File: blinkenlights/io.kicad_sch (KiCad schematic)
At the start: 23 parts, among them J501 Conn_02x10_Odd_Even, U501 XRA1403, U502 PCA9306DP, U503 XRA1403, U504 XRA1402

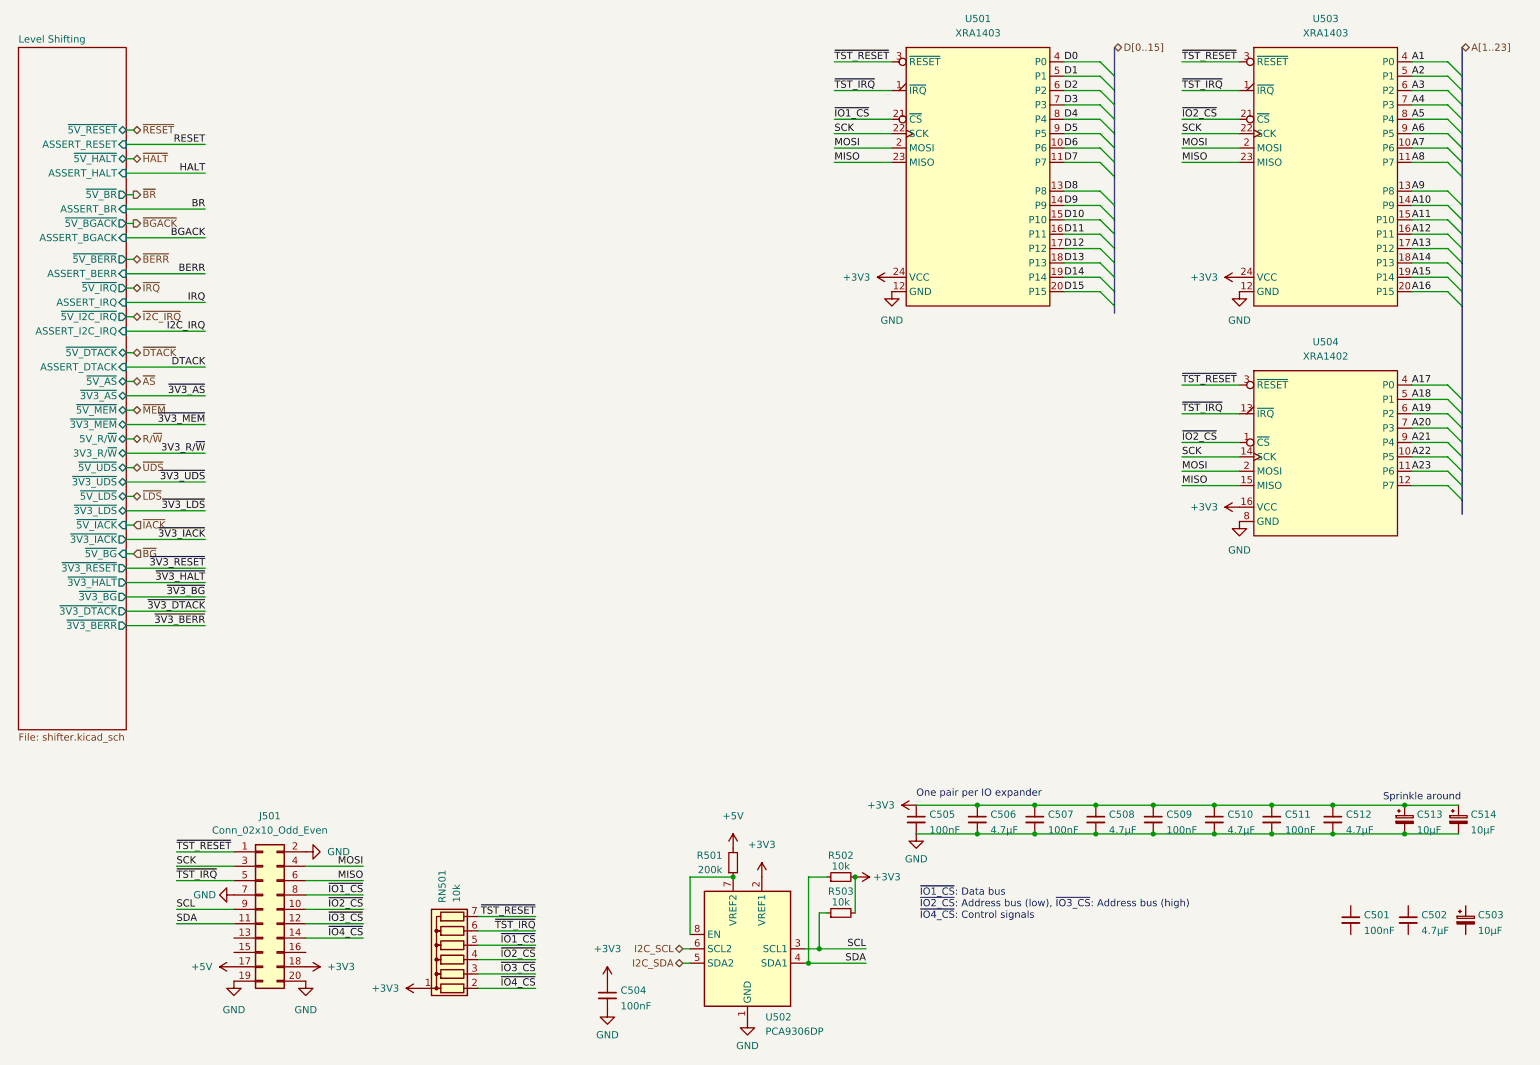
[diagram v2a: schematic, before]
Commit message: Routed control signals
- The blinkenlights board now has the control signals routed to IO
  expanders, and removed a bunch of superfluous level shifting type
  stuff
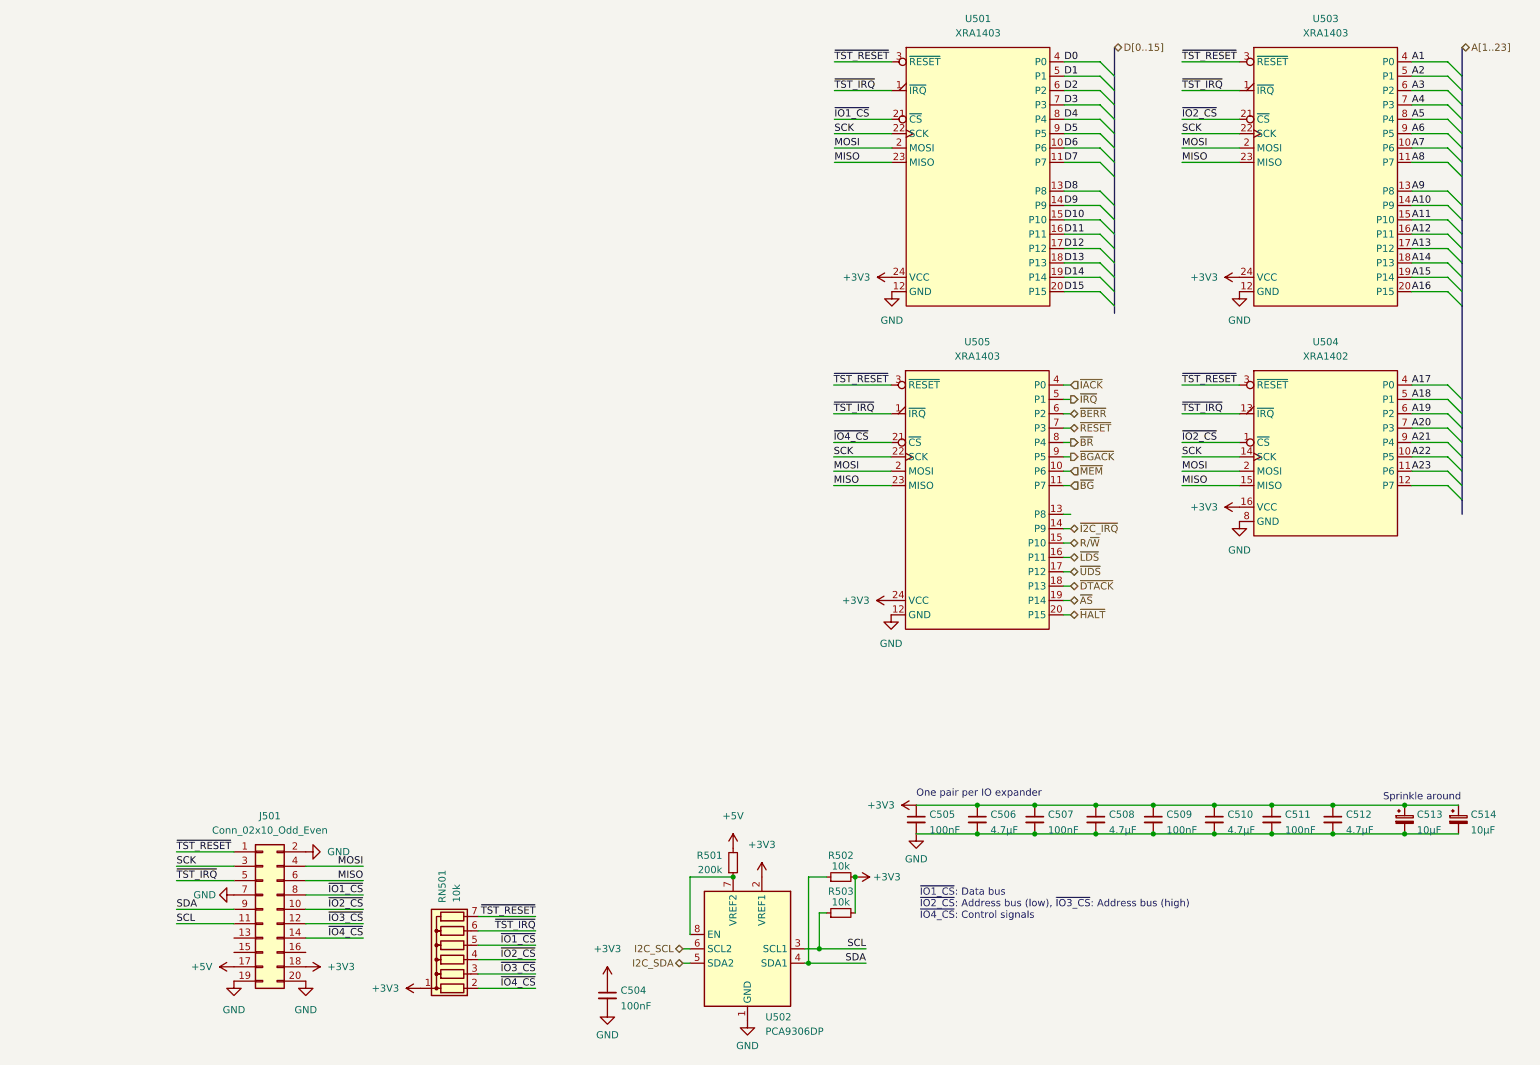
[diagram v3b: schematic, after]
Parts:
- removed C501: 100nF, Capacitor_SMD:C_0805_2012Metric, symbol Device:C_Small
- removed C502: 4.7µF, Capacitor_SMD:C_0805_2012Metric, symbol Device:C_Small
- removed C503: 10µF, Capacitor_Tantalum_SMD:CP_EIA-3528-21_Kemet-B, symbol Device:C_Polarized_Small
- added U505: XRA1403, Package_SO:TSSOP-24_4.4x7.8mm_P0.65mm, symbol 68komputer-common:XRA1403
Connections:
- net +3V3: now also U505.24 (VCC)
- net GND: now also U505.12 (GND)
- net MISO: now also U505.23 (MISO)
- net MOSI: now also U505.2 (MOSI)
- net R/~{W}: now also U505.15 (P10)
- net SCK: now also U505.22 (SCK)
- net SCL: now also J501.11 (Pin_11); no longer J501.9 (Pin_9)
- net SDA: now also J501.9 (Pin_9); no longer J501.11 (Pin_11)
- net ~{AS}: now also U505.19 (P14)
- net ~{BERR}: now also U505.6 (P2)
- net ~{BGACK}: now also U505.9 (P5)
- net ~{BG}: now also U505.11 (P7)
- net ~{BR}: now also U505.8 (P4)
- net ~{DTACK}: now also U505.18 (P13)
- net ~{HALT}: now also U505.20 (P15)
- net ~{I2C_IRQ}: now also U505.14 (P9)
- net ~{IACK}: now also U505.4 (P0)
- net ~{IO4_CS}: now also U505.21 (~{CS})
- net ~{IRQ}: now also U505.5 (P1)
- net ~{LDS}: now also U505.16 (P11)
- net ~{MEM}: now also U505.10 (P6)
- net ~{RESET}: now also U505.7 (P3)
- net ~{TST_IRQ}: now also U505.1 (~{IRQ})
- net ~{TST_RESET}: now also U505.3 (~{RESET})
- net ~{UDS}: now also U505.17 (P12)
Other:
- removed sheet Level Shifting

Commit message: Mostly finished blinkenlights contraption
- Added some headers that can have logic probes connected to them; we
  need to route them and ensure the pins are correct
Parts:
- removed C510: 4.7µF, Capacitor_SMD:C_0805_2012Metric, symbol Device:C_Small
- removed C513: 10µF, Capacitor_Tantalum_SMD:CP_EIA-3528-21_Kemet-B, symbol Device:C_Polarized_Small
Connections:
- net ~{IO1_CS}: now also J501.14 (Pin_14), RN501.2 (R1); no longer J501.8 (Pin_8), RN501.5 (R4)
- net ~{IO2_CS}: now also J501.12 (Pin_12), RN501.3 (R2); no longer J501.10 (Pin_10), RN501.4 (R3), U504.1 (~{CS})
- net ~{IO3_CS}: now also J501.10 (Pin_10), RN501.4 (R3), U504.1 (~{CS}); no longer J501.12 (Pin_12), RN501.3 (R2)
- net ~{IO4_CS}: now also J501.8 (Pin_8), RN501.5 (R4); no longer J501.14 (Pin_14), RN501.2 (R1)
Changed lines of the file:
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@@
   (junction (at 219.71 153.035) (diameter 0) (color 0 0 0 0)
   )
-  (junction (at 230.505 158.115) (diameter 0) (color 0 0 0 0)
-  )
-  (junction (at 264.16 153.035) (diameter 0) (color 0 0 0 0)
-  )
-  (junction (at 230.505 153.035) (diameter 0) (color 0 0 0 0)
-  )
-  (junction (at 264.16 158.115) (diameter 0) (color 0 0 0 0)
-  )
   (junction (at 209.55 153.035) (diameter 0) (color 0 0 0 0)
   )
@@
     (stroke (width 0) (type default) (color 0 0 0 0))
   )
-  (wire (pts (xy 264.16 153.035) (xy 273.685 153.035))
+  (wire (pts (xy 251.46 153.035) (xy 273.685 153.035))
     (stroke (width 0) (type default) (color 0 0 0 0))
   )
@@
     (stroke (width 0) (type default) (color 0 0 0 0))
   )
-  (wire (pts (xy 251.46 153.035) (xy 264.16 153.035))
-    (stroke (width 0) (type default) (color 0 0 0 0))
-  )
   (wire (pts (xy 203.835 96.52) (xy 205.105 96.52))
     (stroke (width 0) (type default) (color 0 0 0 0))
@@
     (stroke (width 0) (type default) (color 0 0 0 0))
   )
-  (wire (pts (xy 251.46 158.115) (xy 264.16 158.115))
-    (stroke (width 0) (type default) (color 0 0 0 0))
-  )
   (bus (pts (xy 212.852 52.07) (xy 212.852 54.61))
     (stroke (width 0) (type default) (color 0 0 0 0))
@@
     (stroke (width 0) (type default) (color 0 0 0 0))
   )
-  (wire (pts (xy 230.505 158.115) (xy 240.665 158.115))
-    (stroke (width 0) (type default) (color 0 0 0 0))
-  )
   (wire (pts (xy 271.78 93.98) (xy 265.43 93.98))
     (stroke (width 0) (type default) (color 0 0 0 0))
@@
     (stroke (width 0) (type default) (color 0 0 0 0))
   )
-  (wire (pts (xy 219.71 158.115) (xy 230.505 158.115))
+  (wire (pts (xy 219.71 158.115) (xy 240.665 158.115))
     (stroke (width 0) (type default) (color 0 0 0 0))
   )
@@
     (stroke (width 0) (type default) (color 0 0 0 0))
   )
-  (wire (pts (xy 230.505 153.035) (xy 240.665 153.035))
+  (wire (pts (xy 219.71 153.035) (xy 240.665 153.035))
     (stroke (width 0) (type default) (color 0 0 0 0))
   )
@@
     (stroke (width 0) (type default) (color 0 0 0 0))
   )
-  (wire (pts (xy 219.71 153.035) (xy 230.505 153.035))
-    (stroke (width 0) (type default) (color 0 0 0 0))
-  )
   (wire (pts (xy 224.79 88.9) (xy 234.95 88.9))
     (stroke (width 0) (type default) (color 0 0 0 0))
@@
     (stroke (width 0) (type default) (color 0 0 0 0))
   )
-  (wire (pts (xy 264.16 158.115) (xy 273.685 158.115))
+  (wire (pts (xy 251.46 158.115) (xy 273.685 158.115))
     (stroke (width 0) (type default) (color 0 0 0 0))
   )
@@
     (effects (font (size 1.27 1.27)) (justify left bottom))
   )
-  (label "~{IO2_CS}" (at 80.01 171.45 180)
+  (label "~{IO3_CS}" (at 80.01 171.45 180)
     (effects (font (size 1.27 1.27)) (justify right bottom))
   )
@@
     (effects (font (size 1.27 1.27)) (justify left bottom))
   )
-  (label "~{IO3_CS}" (at 80.01 173.99 180)
+  (label "~{IO2_CS}" (at 80.01 173.99 180)
     (effects (font (size 1.27 1.27)) (justify right bottom))
   )
@@
     (effects (font (size 1.27 1.27)) (justify left bottom))
   )
-  (label "~{IO4_CS}" (at 110.49 185.42 180)
+  (label "~{IO4_CS}" (at 110.49 177.8 180)
     (effects (font (size 1.27 1.27)) (justify right bottom))
   )
-  (label "~{IO1_CS}" (at 110.49 177.8 180)
+  (label "~{IO1_CS}" (at 110.49 185.42 180)
     (effects (font (size 1.27 1.27)) (justify right bottom))
   )
@@
     (effects (font (size 1.27 1.27)) (justify left bottom))
   )
-  (label "~{IO2_CS}" (at 224.79 88.9 0)
+  (label "~{IO3_CS}" (at 224.79 88.9 0)
     (effects (font (size 1.27 1.27)) (justify left bottom))
   )
@@
     (effects (font (size 1.27 1.27)) (justify left bottom))
   )
-  (label "~{IO2_CS}" (at 110.49 180.34 180)
+  (label "~{IO3_CS}" (at 110.49 180.34 180)
     (effects (font (size 1.27 1.27)) (justify right bottom))
   )
@@
     (effects (font (size 1.27 1.27)) (justify left bottom))
   )
-  (label "~{IO1_CS}" (at 80.01 168.91 180)
+  (label "~{IO4_CS}" (at 80.01 168.91 180)
     (effects (font (size 1.27 1.27)) (justify right bottom))
   )
@@
     (effects (font (size 1.27 1.27)) (justify left bottom))
   )
-  (label "~{IO3_CS}" (at 110.49 182.88 180)
+  (label "~{IO2_CS}" (at 110.49 182.88 180)
     (effects (font (size 1.27 1.27)) (justify right bottom))
   )
@@
     (effects (font (size 1.27 1.27)) (justify left bottom))
   )
-  (label "~{IO4_CS}" (at 80.01 176.53 180)
+  (label "~{IO1_CS}" (at 80.01 176.53 180)
     (effects (font (size 1.27 1.27)) (justify right bottom))
   )
@@
   (hierarchical_label "~{AS}" (shape bidirectional) (at 205.105 116.84 0)
     (effects (font (size 1.27 1.27)) (justify left))
-  )
-  (symbol (lib_id "Device:C_Small") (at 230.505 155.575 0) (unit 1)
-    (in_bom yes) (on_board yes) (fields_autoplaced)
-    (property "Reference" "C510" (id 0) (at 232.8291 154.6665 0)
-      (effects (font (size 1.27 1.27)) (justify left))
-    )
-    (property "Value" "4.7µF" (id 1) (at 232.8291 157.4416 0)
-      (effects (font (size 1.27 1.27)) (justify left))
-    )
-    (property "Footprint" "Capacitor_SMD:C_0805_2012Metric" (id 2) (at 230.505 155.575 0)
-      (effects (font (size 1.27 1.27)) hide)
-    )
-    (property "Datasheet" "~" (id 3) (at 230.505 155.575 0)
-      (effects (font (size 1.27 1.27)) hide)
-    )
-    (pin "1")
-    (pin "2")
   )
   (symbol (lib_id "Device:R_Network06") (at 95.25 177.8 90) (unit 1)
@@
     (pin "1")
   )
-  (symbol (lib_id "Device:C_Polarized_Small") (at 264.16 155.575 0) (unit 1)
-    (in_bom yes) (on_board yes) (fields_autoplaced)
-    (property "Reference" "C513" (id 0) (at 266.319 154.6665 0)
-      (effects (font (size 1.27 1.27)) (justify left))
-    )
-    (property "Value" "10µF" (id 1) (at 266.319 157.4416 0)
-      (effects (font (size 1.27 1.27)) (justify left))
-    )
-    (property "Footprint" "Capacitor_Tantalum_SMD:CP_EIA-3528-21_Kemet-B" (id 2) (at 264.16 155.575 0)
-      (effects (font (size 1.27 1.27)) hide)
-    )
-    (property "Datasheet" "~" (id 3) (at 264.16 155.575 0)
-      (effects (font (size 1.27 1.27)) hide)
-    )
-    (property "MPN" "TAJB106K025SNJ" (id 4) (at 264.16 155.575 0)
-      (effects (font (size 1.27 1.27)) hide)
-    )
-    (pin "1")
-    (pin "2")
-  )
   (symbol (lib_id "power:GND") (at 177.8 158.115 0) (unit 1)

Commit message: Added Teensy, logic probe ports to blinkenlights
- A teensy 4.0 is on board connected to the IO expanders (and directly,
  the /HALT line, so it can single step the CPU on request) rather than
  expecting an external connection.

- Routed all bus signals to the logic analyzer connectors. They're meant
  to connect to a 16700-series pod connector on a 0.1" spacing, with 16
  signal lines, and one clock (CLK) with all other pins tied to ground.
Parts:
- removed J501: Conn_02x10_Odd_Even, Connector_PinHeader_2.54mm:PinHeader_2x10_P2.54mm_Vertical, symbol Connector_Generic:Conn_02x10_Odd_Even
- removed RN501: 10k, Resistor_THT:R_Array_SIP7, symbol Device:R_Network06
- added U506: Teensy4.0, 68komputer-common:Teensy40-NoBonus, symbol teensy:Teensy4.0
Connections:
- net +3V3: now also U506.31 (3V3)
- net +5V: now also U506.33 (VIN)
- net GND: now also U506.1 (GND), U506.17 (GND), U506.32 (GND), U506.47 (GND)
- net MISO: now also U506.14 (12_MISO_MQSL)
- net MOSI: now also U506.13 (11_MOSI_CTX1)
- net SCK: now also U506.20 (13_SCK_CRX1_LED)
- net SCL: now also U506.26 (19_A5_SCL0)
- net SDA: now also U506.25 (18_A4_SDA0)
- net ~{IO1_CS}: now also U506.9 (7_RX2_OUT1A)
- net ~{IO2_CS}: now also U506.10 (8_TX2_IN1)
- net ~{IO3_CS}: now also U506.11 (9_OUT1C)
- net ~{IO4_CS}: now also U506.12 (10_CS_MQSR)
- net ~{TST_IRQ}: now also U506.23 (16_A2_RX4_SCL1)
- net ~{TST_RESET}: now also U506.24 (17_A3_TX4_SDA1)
